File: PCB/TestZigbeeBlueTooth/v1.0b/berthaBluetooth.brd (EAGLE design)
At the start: 96.7 x 71.9 mm, 55 parts, among them CON1 SPI, Q1 BSP75, Q2 BSP75, Q4 BSP75, Q7 BSP75, X3 16MHz, X4 MINI-USB

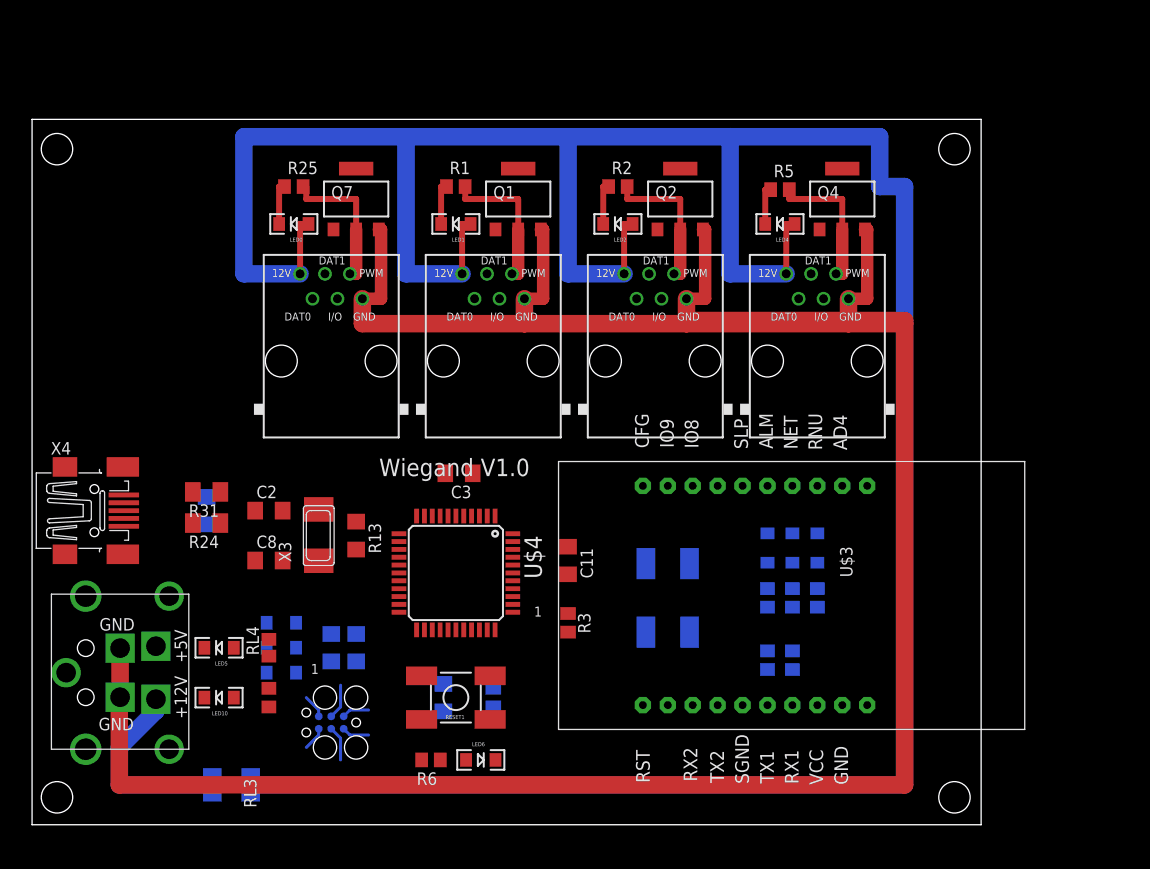
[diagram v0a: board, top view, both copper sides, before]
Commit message: Add relay card and integrated bioreactor
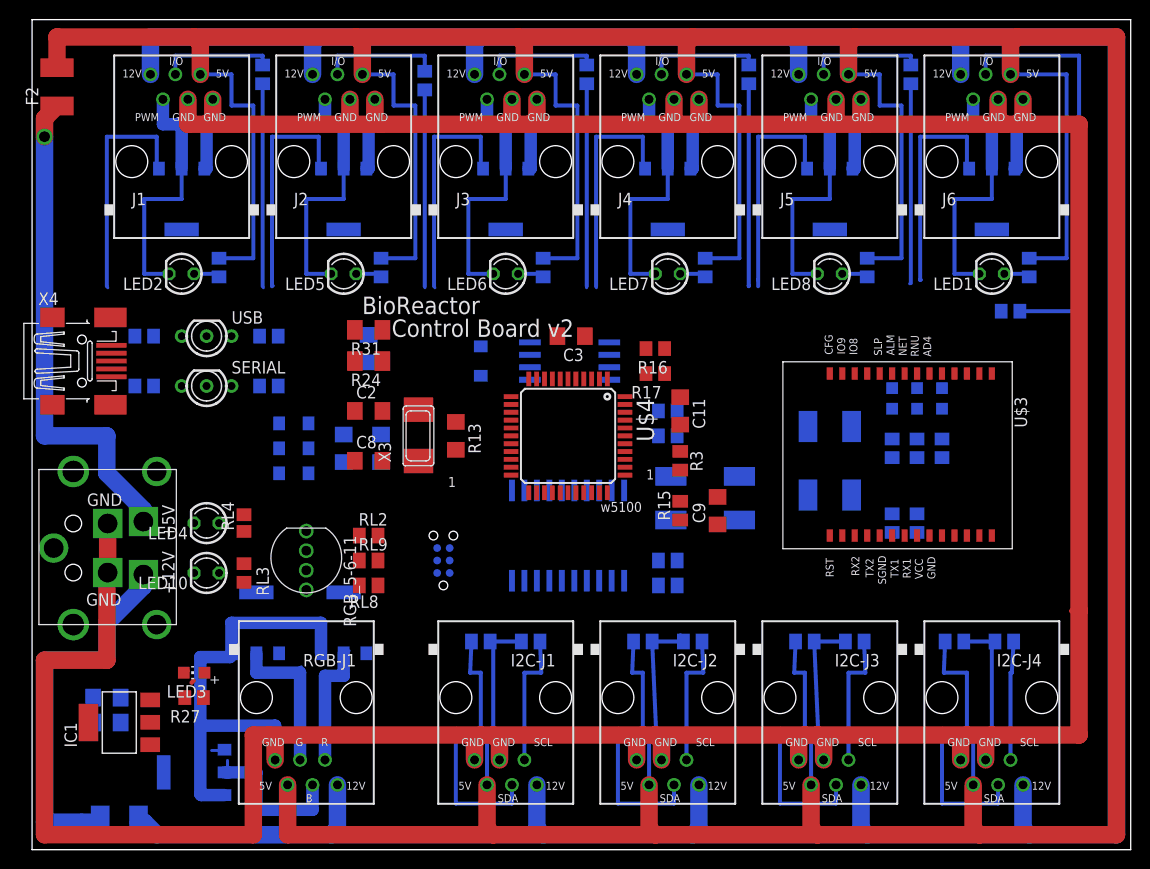
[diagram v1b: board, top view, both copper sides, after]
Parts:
- removed DOOR0, DOOR1, DOOR2, DOOR4: RJ12, lpatiny:RJ12-STRAIGHT-WIEGAND
- removed LED0: Blue, SparkFun:LED-1206
- removed Q7: BSP75, infineon:PG-SOT-223
- removed R2: 10k, rcl:R0805
- added C1, C5: 10uF, rcl:C1206
- added D5: 1N581D1206, lpatiny:LED-1206
- added F2: 0.5A, lpatiny:C1812
- added I2C-J1, I2C-J2, I2C-J3, I2C-J4: RJ12STRAIGHT-I2C, lpatiny:RJ12-STRAIGHT-I2C
- added IC1: REG1117, burr-brown:SOT223
- added J1, J2, J3, J4, J5, J6: RJ12, lpatiny:RJ12-STRAIGHT
- added LED3: RED, adafruit:CHIP-LED0805
- added LED7: BLue, lpatiny:LED3MM
- added LED8: Blue, lpatiny:LED3MM
- added Q10, Q3, Q5, Q6, Q8, Q9: BSP75, infineon:PG-SOT-223
- added R, R17, R19, R20, R32, R33, R34, R35, R4, R7: 1k, rcl:R0805
- added R16, R18: 10k, rcl:R0805
- added R21, R22, R23, R26, R28, R29, R30, R36, R37, R38: 10K, resistor:M0805
- added R27, RL1, RL5, RL6, RL7: 1K, rcl:R0805
- added RGB-J1: RJ12, lpatiny:RJ12-STRAIGHT-RGB
- added RGB_5-6-11: (no value), lpatiny:LED-TRICOLOR-THROUGHHOLE
- added RL2, RL8, RL9: 1K, resistor:M0805
- added SERIAL: BICOLOR-LED, lpatiny:BICOLOR-3MM
- added U$1: SST25VF064C, BertaLib:SOIC_8-LEAD
- added U$2: PCA9518, lpatiny:SO20W
- added USB: BICOLOR-LED COMMON CAT, lpatiny:BICOLOR-3MM
- CON1: device lpatiny:TC2030-MCP -> lpatiny:TC2030-MCP-NL
- LED1, LED10, LED2: device SparkFun:LED-1206 -> lpatiny:LED3MM
- LED11, LED12, LED9: device SparkFun:LED-1206 -> adafruit:CHIP-LED0805
- LED4: value Blue -> RED; device SparkFun:LED-1206 -> lpatiny:LED3MM
- LED5, LED6: value RED -> Blue; device SparkFun:LED-1206 -> lpatiny:LED3MM
- R25, R5: value 10k -> 1k
- R6: value 1K -> 1k
- U$3: value SZ05-ZIGBEE -> SZ05-ZIGBEESMD; device lpatiny:SZ05-ZIGBEE -> lpatiny:SZ05-ZIGBEE3
- U$4: value ATMEGA32U4 -> ATMEGA32U4-AU
- moved LED4 65.9 mm to (17.8, 30.5)
- moved R6 57.4 mm to (68.6, 56.5), flipped to the bottom, turned to 90 degrees
- moved LED1 54.8 mm to (97.8, 55.9)
- moved LED6 49.6 mm to (48.3, 55.9), turned to 180 degrees
- moved LED2 44.7 mm to (15.2, 55.9)
- moved LED5 40.2 mm to (31.8, 55.9)
- moved Q2 34.3 mm to (31.8, 63.5), flipped to the bottom, turned to 180 degrees
- moved Q1 34.3 mm to (15.2, 63.5), flipped to the bottom, turned to 180 degrees
- moved Q4 34.3 mm to (48.3, 63.5), flipped to the bottom, turned to 180 degrees
- moved C9 33.8 mm to (69.8, 31.8), flipped to the top
- moved R1 33.3 mm to (64.8, 39.4), flipped to the bottom, turned to 180 degrees
- moved RESET1 32.5 mm to (68.6, 33.0), flipped to the bottom
- moved R15 26.9 mm to (66.0, 31.8), flipped to the top
- moved R5 25.4 mm to (52.1, 56.5), flipped to the bottom, turned to 90 degrees
- moved U$3 23.4 mm to (88.9, 38.1)
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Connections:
- removed net +5V1: R6.2
- removed net D2*: DOOR0.DAT0, U$4.19
- removed net D3*: DOOR0.DAT1, U$4.18
- removed net N$31: DOOR4.PWM, Q4.2, R5.2
- new net 3.3V: C1.1, IC1.2, R1.2, R16.2, R27.2, U$1.RST/HOLD, U$1.VDD, U$1.WP, U$2.20
- new net FMOSI: D5.A, R1.1, U$1.SI
- new net N$10: R16.1, R17.1, U$1.CE
- new net N$13: RL5.2, SERIAL.3
- new net N$14: RL7.2, USB.1
- new net N$15: RL6.2, SERIAL.1
- new net N$17: LED2.A, R25.1
- new net N$18: J1.I/O, R.2
- new net N$19: J5.PWM, LED8.K, Q6.2
- new net N$20: LED3.A, R27.1
- new net N$21: J6.PWM, LED1.K, Q3.2
- new net N$22: LED6.A, R5.1
- new net N$28: J2.PWM, LED5.K, Q2.2
- new net N$29: J4.I/O, R34.2
- new net N$30: LED7.A, R6.1
- new net N$32: J5.I/O, R35.2
- new net N$33: LED8.A, R7.1
- new net N$34: J1.PWM, LED2.K, Q1.2
- new net N$36: RGB_5-6-11.RED, RL2.2
- new net N$37: RGB_5-6-11.BLU, RL8.2
- new net N$38: F2.1, U$6.+5V
- new net N$4: LED5.A, R4.1
- new net N$40: RGB_5-6-11.GRN, RL9.2
- new net N$50: Q9.2, RGB-J1.B, RL8.1
- new net N$68: Q8.2, RGB-J1.R, RL2.1
- new net N$8: RL1.2, USB.3
- new net SCL: R28.2, U$2.3, U$4.18
- new net SCL1: I2C-J4.SCL, R30.2, U$2.5
- new net SCL2: I2C-J3.SCL, R37.1, U$2.8
- new net SCL3: I2C-J2.SCL, R22.1, U$2.12
- new net SCL4: I2C-J1.SCL, R23.1, U$2.15
- new net SDA: R29.2, U$2.4, U$4.19
- new net SDA1: I2C-J4.SDA, R36.1, U$2.6
- new net SDA2: I2C-J3.SDA, R38.1, U$2.9
- new net SDA3: I2C-J2.SDA, R26.1, U$2.13
- new net SDA4: I2C-J1.SDA, R21.2, U$2.16
- net +12V: now also I2C-J1.+12V, I2C-J2.+12V, I2C-J3.+12V, I2C-J4.+12V, J1.+12V, J2.+12V, J3.+12V, J4.+12V, J5.+12V, J6.+12V, RGB-J1.+12V; no longer DOOR0.+12V, DOOR1.+12V, DOOR2.+12V, DOOR4.+12V, LED0.A, LED1.A, LED2.A, LED4.A
- net +5V: now also F2.2, I2C-J1.+5V, I2C-J2.+5V, I2C-J3.+5V, I2C-J4.+5V, J1.+5V, J2.+5V, J3.+5V, J4.+5V, J5.+5V, J6.+5V, R20.2, R21.1, R22.2, R23.2, R25.2, R26.2, R28.1, R29.1, R30.1, R36.2, R37.2, R38.2, R4.2, R5.2, R6.2, R7.2, RGB-J1.+5V, RGB_5-6-11.GND; no longer U$6.+5V
- net +5V/1: now also C5.1, IC1.3
- net A0: now also R35.1; no longer DOOR4.I/O
- net A1: now also R33.1; no longer DOOR2.I/O
- net A2: now also R32.1; no longer DOOR1.I/O
- net A3: now also R.1; no longer DOOR0.I/O
- net A4: now also R34.1
- net A5: now also R19.1
- net CS: now also R17.2
- net D10*: now also Q3.1; no longer DOOR2.DAT0
- net D11*: now also Q6.1; no longer DOOR2.DAT1
- net D12*: now also Q8.1; no longer Q4.1
- net D13*: now also Q9.1; no longer Q2.1
- net D5*: now also Q5.1; no longer Q1.1
- net D6*: now also Q1.1; no longer Q7.1
- net D7*: now also Q10.1
- net D8*: now also Q2.1; no longer DOOR1.DAT0
- net D9*: now also Q4.1; no longer DOOR1.DAT1
- net GND: now also C1.2, C5.2, I2C-J1.GND1, I2C-J1.GND2, I2C-J2.GND1, I2C-J2.GND2, I2C-J3.GND1, I2C-J3.GND2, I2C-J4.GND1, I2C-J4.GND2, IC1.1, J1.GND1, J1.GND2, J2.GND1, J2.GND2, J3.GND1, J3.GND2, J4.GND1, J4.GND2, J5.GND1, J5.GND2, J6.GND1, J6.GND2, LED10.K, LED3.C, LED4.K, Q10.3, Q3.3, Q5.3, Q6.3, Q8.3, Q9.3, RGB-J1.GND1, SERIAL.2, U$1.VSS, U$2.10, U$3.SND, USB.2; no longer DOOR0.GND, DOOR1.GND, DOOR2.GND, DOOR4.GND, LED10.C, LED5.C, LED6.C, Q7.3, U$3.SGND
- net GND1: now also U$3.RUN; no longer U$3.RNU
- net MISO: now also U$1.SO; no longer DOOR4.DAT1
- net MOSI: now also D5.C
- net N$1: now also J3.PWM, LED6.K, Q4.2; no longer LED0.C, R25.1
- net N$12: now also LED4.A; no longer LED5.A
- net N$2: now also J2.I/O, R32.2; no longer LED6.A, R6.1
- net N$23: now also R18.2, U$1.SCK; no longer DOOR0.PWM, Q7.2, R25.2
- net N$3: now also J6.I/O, R19.2; no longer DOOR1.PWM, Q1.2, R1.2
- net N$5: now also J4.PWM, LED7.K, Q5.2; no longer LED1.C, R1.1
- net N$6: now also Q10.2, RGB-J1.G, RL9.1; no longer LED2.C, R2.1
- net N$7: now also J3.I/O, R33.2; no longer DOOR2.PWM, Q2.2, R2.2
- net N$9: now also LED1.A, R20.1; no longer LED4.C, R5.1
- net RD+: now also RL7.1
- net RD-: now also RL1.1
- net RXLED: now also RL5.1
- net SCK: now also R18.1; no longer DOOR4.DAT0
- net TXLED: now also RL6.1
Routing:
- net +5V: track 0.00 -> 570.8 mm
- net GND: track 269.0 -> 462.8 mm
- net N$38: track 0.00 -> 50.8 mm, vias 0 -> 1
- net N$3: track 14.9 -> 59.1 mm
- net SDA1: track 0.00 -> 29.2 mm
- net +12V: track 302.5 -> 330.8 mm
- net SDA2: track 0.00 -> 27.9 mm
- net SDA3: track 0.00 -> 27.9 mm
- net SDA4: track 0.00 -> 27.8 mm
- net N$19: track 0.00 -> 26.0 mm
- net N$34: track 0.00 -> 26.0 mm
- net N$28: track 0.00 -> 26.0 mm
- net N$21: track 0.00 -> 26.0 mm
- net D6*: track 0.00 -> 24.0 mm
- net D9*: track 0.00 -> 23.7 mm
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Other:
- board size 96.7 x 71.9 mm -> 111.9 x 84.6 mm
- board text added: "BioReactor"
- board text added: "Control Board v2"
- board text added: "w5100"
- board text removed: "Wiegand V1.0"
- board text removed: "Wiegand v1.1"
